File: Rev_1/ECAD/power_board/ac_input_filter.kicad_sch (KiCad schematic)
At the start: 16 parts, among them K1 SPST-NO, Q3 NMOS

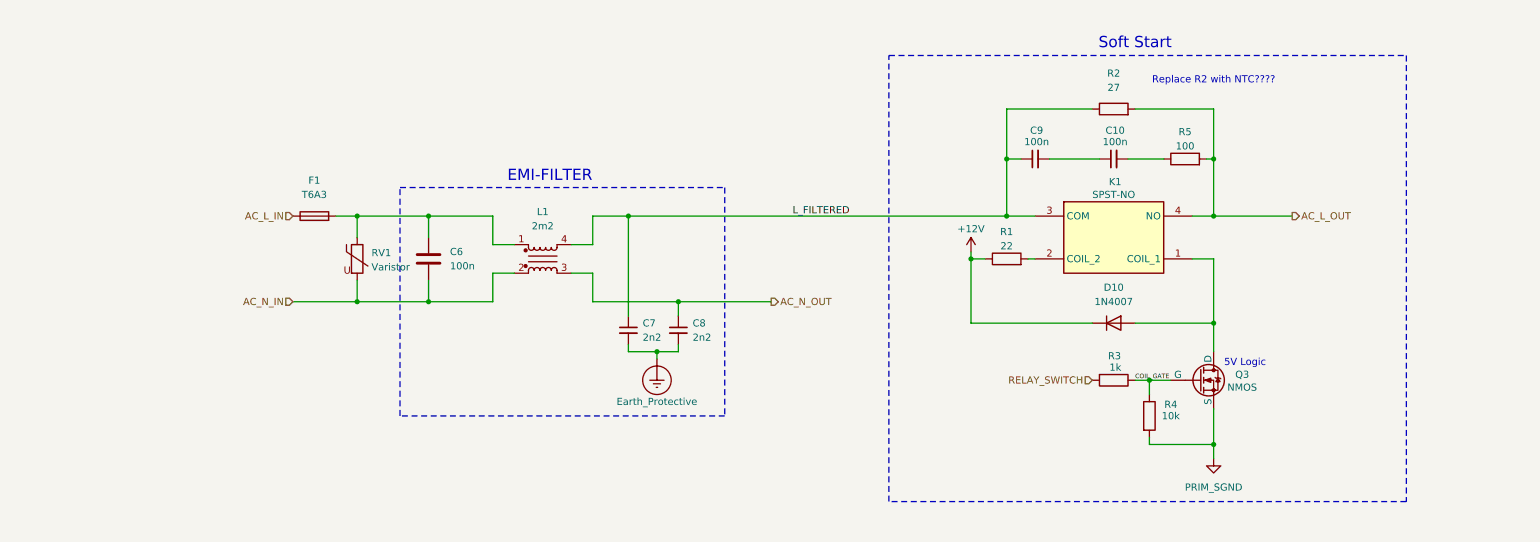
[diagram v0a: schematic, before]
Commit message: Assign footprints
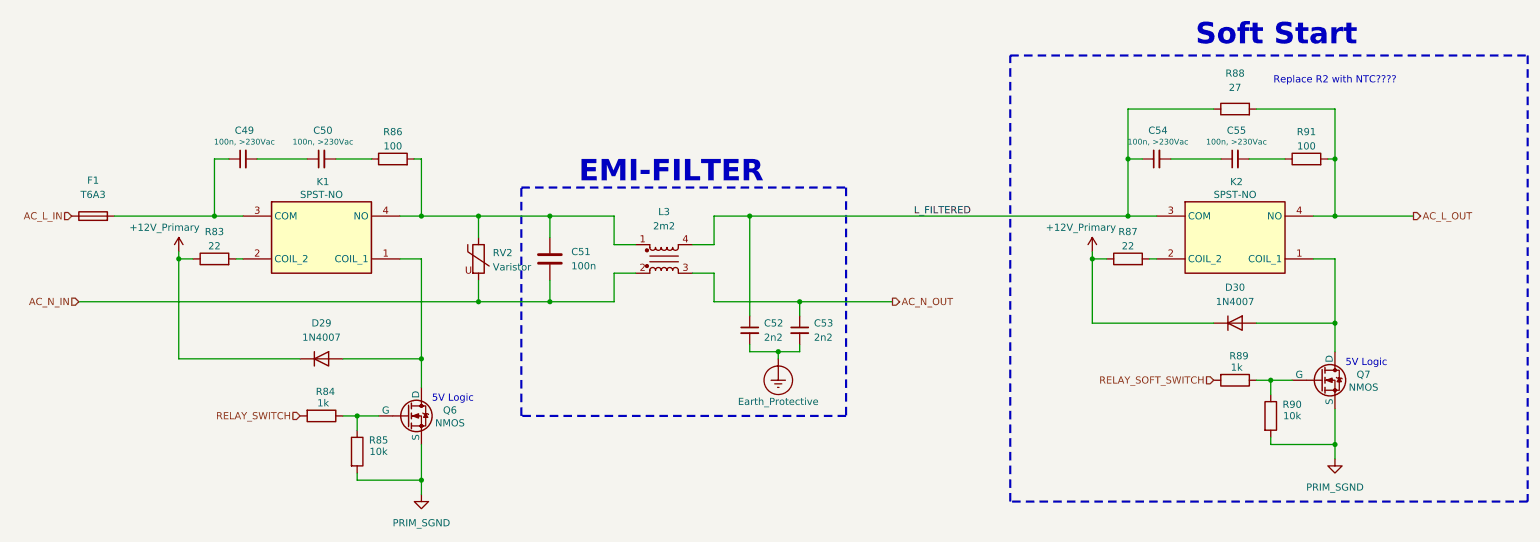
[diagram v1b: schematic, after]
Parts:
- added C49, C50: 100n, >230Vac, symbol Device:C_Small
- added D29: 1N4007, Diode_THT:D_DO-41_SOD81_P10.16mm_Horizontal, symbol Diode:1N4007
- added K1: SPST-NO, filip:Industrial-Relays-OJS-SS-112HEF_SPST-NO, symbol filip:2071556-1
- added Q6: NMOS, symbol Simulation_SPICE:NMOS
- added R83: 22, Resistor_SMD:R_1206_3216Metric, symbol Device:R
- added R84: 1k, Resistor_SMD:R_0805_2012Metric, symbol Device:R
- added R85: 10k, Resistor_SMD:R_0805_2012Metric, symbol Device:R
- added R86: 100, symbol Device:R
- C54: renamed from C9; value 100n -> 100n, >230Vac
- C55: renamed from C10; value 100n -> 100n, >230Vac
- renumbered C6 to C51, C7 to C52, C8 to C53, D10 to D30, K1 to K2, L1 to L3, Q3 to Q7, R1 to R87, R2 to R88, R3 to R89, R4 to R90, R5 to R91, RV1 to RV2
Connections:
- net PRIM_SGND: now also Q6.3 (S), R85.2
- net RELAY_SWITCH: now also R84.2; no longer R89.2
- net at C51.1, L3.1, RV2.1: now also K1.4 (NO), R86.2; no longer F1.2
- net +12V renamed +12V_Primary
- net +12V_Primary: now also D29.1 (K), R83.1
- net COIL_GATE: no longer names the net of Q7.2 (G), R89.1, R90.1
- new net: Q6.2 (G), R84.1, R85.1
- new net: D29.2 (A), K1.1 (COIL_1), Q6.1 (D)
- new net: K1.2 (COIL_2), R83.2
- new net: C49.1, F1.2, K1.3 (COM)
- new net: C49.2, C50.1
- new net: C50.2, R86.1
- new net RELAY_SOFT_SWITCH: R89.2
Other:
- moved on the sheet: C51, C52, C53, C54, C55, D30, F1, K2, L3, Q7, R87, R88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

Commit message: Before PR
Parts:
- C44: renamed from C49; footprint (none) -> Capacitor_THT:C_Rect_L13.0mm_W5.0mm_P10.00mm_FKS3_FKP3_MKS4; Mouser No: 505-MKX2AW31004CMSSD -> 710-890324023023
- C45: renamed from C50; footprint (none) -> Capacitor_THT:C_Rect_L13.0mm_W5.0mm_P10.00mm_FKS3_FKP3_MKS4; Mouser No: 505-MKX2AW31004CMSSD -> 710-890324023023
- C46: renamed from C51; value 100n -> 100n, >230AC
- C47: renamed from C52; Part-DB ID (none) -> 59; Part-DB NAME (none) -> F340Y232230MFP2B0
- C49: renamed from C54; footprint (none) -> Capacitor_THT:C_Rect_L13.0mm_W5.0mm_P10.00mm_FKS3_FKP3_MKS4; Mouser No: 505-MKX2AW31004CMSSD -> 710-890324023023
- C50: renamed from C55; footprint (none) -> Capacitor_THT:C_Rect_L13.0mm_W5.0mm_P10.00mm_FKS3_FKP3_MKS4; Mouser No: 505-MKX2AW31004CMSSD -> 710-890324023023
- K1, K2: Part-DB ID (none) -> 56; Part-DB NAME (none) -> 2071556-1
- L3: Part-DB ID (none) -> 54; Part-DB NAME (none) -> 7448258022
- Q6, Q7: footprint (none) -> Package_TO_SOT_SMD:SOT-23-3; Mouser No: (none) -> 241-PJA3412_R1_00001
- R92: renamed from R84; Part-DB ID (none) -> 66; Part-DB NAME (none) -> 40819310
- R93: renamed from R85; Part-DB ID (none) -> 67; Part-DB NAME (none) -> 40819410
- R94: renamed from R86; value 100 -> 100, >230Vac; footprint (none) -> Resistor_THT:R_Axial_DIN0411_L9.9mm_D3.6mm_P12.70mm_Horizontal; Mouser No: (none) -> 603-CFR-50JR-52-100R
- R96: renamed from R88; Part-DB ID (none) -> 58; Part-DB NAME (none) -> TWW20J27RE
- R97: renamed from R89; Part-DB ID (none) -> 66; Part-DB NAME (none) -> 40819310
- R98: renamed from R90; Part-DB ID (none) -> 67; Part-DB NAME (none) -> 40819410
- R99: renamed from R91; value 100 -> 100, >230Vac; footprint (none) -> Resistor_THT:R_Axial_DIN0411_L9.9mm_D3.6mm_P12.70mm_Horizontal; Mouser No: (none) -> 603-CFR-50JR-52-100R
- RV1: renamed from RV2; footprint (none) -> Varistor:RV_Disc_D15.5mm_W5mm_P7.5mm
- renumbered C53 to C48, D29 to D33, D30 to D34, R83 to R91, R87 to R95
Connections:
- net RELAY_SWITCH_G: now reaches Q6.2 (G), R92.1, R93.1
- net AC_L_INPUT_RELAY: now reaches C46.1, K1.4 (NO), L3.1, R94.2, RV1.1
- net RELAY_SWITCH_D: now reaches D33.2 (A), K1.1 (COIL_1), Q6.1 (D)
- net RELAY1_COIL_2: now reaches K1.2 (COIL_2), R91.2
- net AC_L_FUSED: now reaches C44.1, F1.2, K1.3 (COM)
- net RELAY2_COIL_2: now reaches K2.2 (COIL_2), R95.2
- net AC_RELAY1_RC_SNUBBER_1: now reaches C44.2, C45.1
- net AC_RELAY1_RC_SNUBBER_2: now reaches C45.2, R94.1
- net AC_RELAY2_RC_SNUBBER_1: now reaches C49.2, C50.1
- net AC_RELAY2_RC_SNUBBER_2: now reaches C50.2, R99.1
- net SOFT_SWITCH_D: now reaches D34.2 (A), K2.1 (COIL_1), Q7.1 (D)
- net SOFT_SWITCH_G: now reaches Q7.2 (G), R97.1, R98.1
- net L_FILTERED renamed AC_L_FILTERED
